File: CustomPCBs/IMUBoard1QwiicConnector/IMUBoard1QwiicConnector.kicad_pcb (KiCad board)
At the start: 2 copper layers, 11.1 x 17.7 mm, 14 parts, among them J1 Conn_01x04_Pin, Y1 32.768kHz

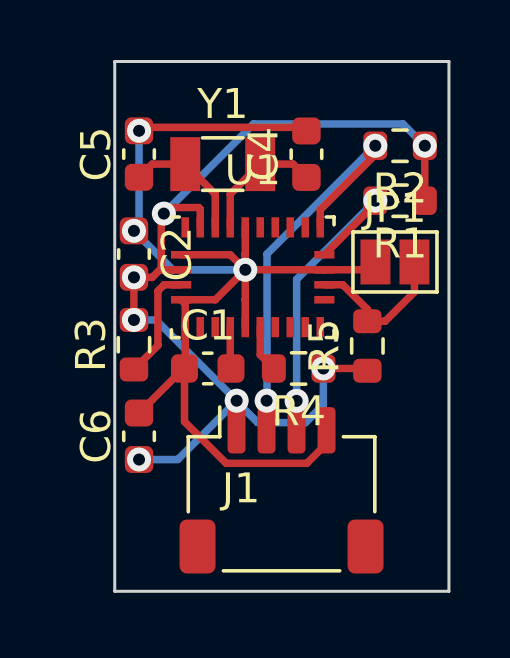
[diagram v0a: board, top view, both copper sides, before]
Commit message: Updating smallest IMU board
Will probably make it even smaller by hardwiring PS0, PS1 and SDO pins.
And maybe even the connector can go to give room for a cable bundle of 4
wires soldered to the board directly.
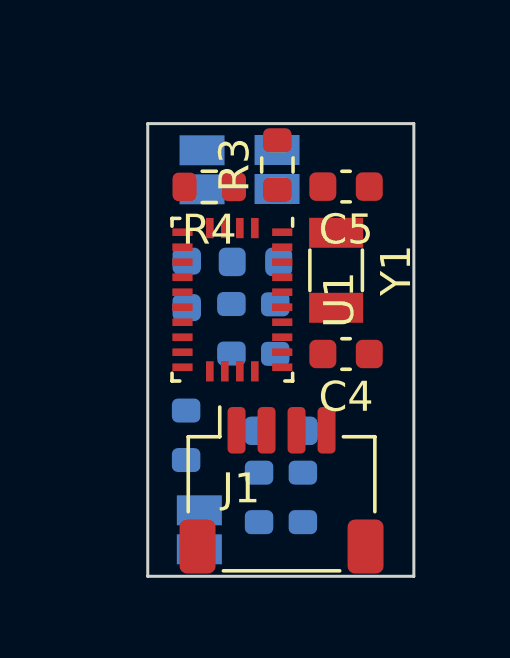
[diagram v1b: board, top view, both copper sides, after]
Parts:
- added JP2: SolderJumper_2_Open, Jumper:SolderJumper-2_P1.3mm_Open_Pad1.0x1.5mm, B.Cu at (97.1, 99.8)
- added JP3: SolderJumper_2_Open, Jumper:SolderJumper-2_P1.3mm_Open_Pad1.0x1.5mm, B.Cu at (99.6, 99.8)
- added R6: 10k, Resistor_SMD:R_0603_1608Metric, B.Cu at (98.1, 105.1)
- added R7: 10k, Resistor_SMD:R_0603_1608Metric, B.Cu at (99.6, 105.1)
- C1, C2, C6, JP1, R1, R2, R5: moved to B.Cu
- moved R2 12.6 mm to (99.0, 110.7), turned to 90 degrees
- moved JP1 11.1 mm to (97.0, 111.8), turned to 90 degrees
- moved R1 10.4 mm to (100.5, 110.7), turned to 90 degrees
- moved R3 7.66 mm to (99.6, 99.7)
- moved C5 6.98 mm to (101.9, 100.4), turned to 180 degrees
- moved C4 6.79 mm to (101.9, 106.0), turned to 180 degrees
- moved R4 6.75 mm to (97.4, 100.4)
- moved R5 6.73 mm to (96.6, 108.7)
- moved Y1 5.18 mm to (101.6, 103.2), turned to -90 degrees
- moved C6 4.73 mm to (99.8, 108.5), turned to 0 degrees
- moved C2 4.06 mm to (98.9, 102.9), turned to 180 degrees
- moved C1 2.89 mm to (96.6, 103.6), turned to 90 degrees
- moved U1 1.01 mm to (98.1, 104.1), turned to -90 degrees
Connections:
- U1 pad 5: GND -> PS1
- U1 pad 6: GND -> PS0
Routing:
- net GND: track 38.3 -> 0.00 mm, vias 3 -> 0
- net +3V3: track 34.6 -> 0.00 mm, vias 7 -> 0
- net SDA: track 14.8 -> 0.00 mm, vias 2 -> 0
- net SCL: track 11.2 -> 0.00 mm, vias 2 -> 0
- net SDO: track 5.14 -> 0.00 mm
- net Net-(U1-CLKSEL1/XOUT32): track 4.25 -> 0.00 mm
- net Net-(U1-XIN32): track 4.25 -> 0.00 mm
- net Net-(U1-BOOTN): track 3.81 -> 0.00 mm
- net Net-(U1-NRST): track 1.57 -> 0.00 mm
- net Net-(U1-CAP): track 1.39 -> 0.00 mm
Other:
- board size 11.1 x 17.7 mm -> 8.9 x 15.1 mm

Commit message: Making the IMU board on the finger tip smaller
Just saving work to continue at lunch, will use 4 layer pcb for the
board to be as small as possible
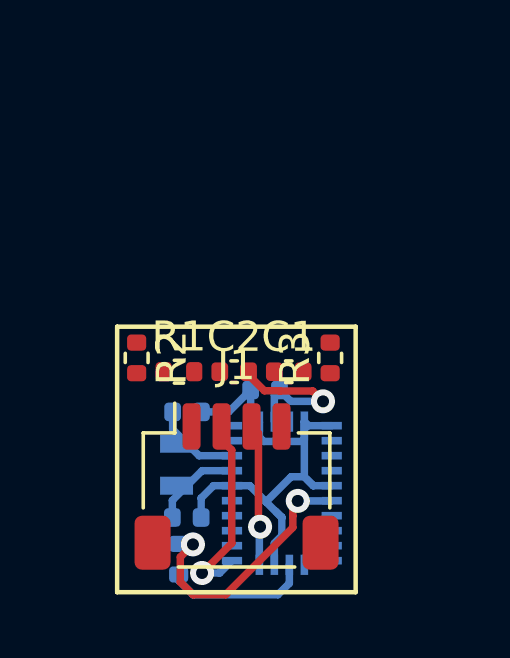
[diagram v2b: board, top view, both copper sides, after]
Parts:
- removed JP1, JP2, JP3: SolderJumper_2_Open, Jumper:SolderJumper-2_P1.3mm_Open_Pad1.0x1.5mm
- removed R5, R6, R7: 10k, Resistor_SMD:R_0603_1608Metric
- C1, C2: footprint Capacitor_SMD:C_0603_1608Metric -> Capacitor_SMD:C_0402_1005Metric; moved to F.Cu
- C4, C5: footprint Capacitor_SMD:C_0603_1608Metric -> Capacitor_SMD:C_0402_1005Metric; moved to B.Cu
- C6: footprint Capacitor_SMD:C_0603_1608Metric -> Capacitor_SMD:C_0402_1005Metric
- R1, R2: footprint Resistor_SMD:R_0603_1608Metric -> Resistor_SMD:R_0402_1005Metric; moved to F.Cu
- R3: footprint Resistor_SMD:R_0603_1608Metric -> Resistor_SMD:R_0402_1005Metric
- R4: footprint Resistor_SMD:R_0603_1608Metric -> Resistor_SMD:R_0402_1005Metric; moved to B.Cu
- U1: moved to B.Cu
- Y1: footprint Crystal:Crystal_SMD_3215-2Pin_3.2x1.5mm -> Crystal:Crystal_SMD_2012-2Pin_2.0x1.2mm; moved to B.Cu
- moved R4 12.5 mm to (96.3, 112.8), turned to 90 degrees
- moved C5 9.19 mm to (96.6, 107.9), turned to 0 degrees
- moved Y1 8.38 mm to (96.3, 109.6), turned to 90 degrees
- moved C4 7.61 mm to (96.6, 111.4), turned to 0 degrees
- moved R3 6.67 mm to (101.4, 106.1)
- moved U1 6.66 mm to (99.8, 110.6)
- moved R2 6.19 mm to (95.0, 106.1), turned to -90 degrees
- moved R1 5.88 mm to (96.4, 106.5), turned to 0 degrees
- moved C1 4.48 mm to (100.0, 106.5), turned to 0 degrees
- moved C2 3.73 mm to (98.2, 106.5), turned to 0 degrees
- moved J1 1.51 mm to (98.3, 110.4)
- moved C6 1.46 mm to (99.2, 107.2), turned to 180 degrees
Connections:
- U1 pad 17: SDO -> +3V3
- U1 pad 5: PS1 -> GND
- U1 pad 6: PS0 -> GND
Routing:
- net GND: track 0.00 -> 17.5 mm
- net +3V3: track 0.00 -> 10.5 mm, vias 0 -> 1
- net Net-(U1-NRST): track 0.00 -> 8.37 mm, vias 0 -> 2
- net SDA: track 0.00 -> 6.60 mm, vias 0 -> 1
- net SCL: track 0.00 -> 4.74 mm, vias 0 -> 1
- net Net-(U1-CLKSEL1/XOUT32): track 0.00 -> 2.97 mm
- net Net-(U1-XIN32): track 0.00 -> 2.92 mm
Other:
- board outline removed
- copper layers 2 -> 4

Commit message: Smaller IMU board achieved, needs centering
So it is possible to get a JST and BNO085 in a board around 9x8mm. This
looks good enough for the finger tip
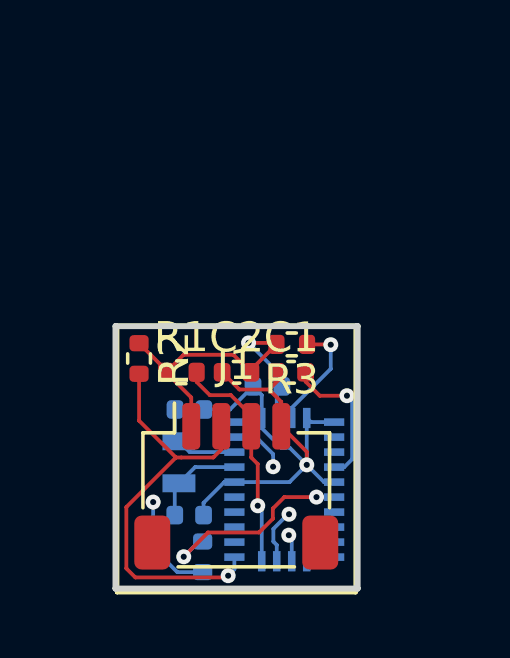
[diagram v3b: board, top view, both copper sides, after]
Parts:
- moved R3 1.36 mm to (100.1, 105.6), turned to 180 degrees
- moved R4 0.80 mm to (97.2, 112.7)
- moved C6 0.14 mm to (99.3, 107.0)
- moved U1 0.14 mm to (99.9, 110.5)
- moved C4 0.11 mm to (96.7, 111.3)
- moved C5 0.11 mm to (96.7, 107.8)
- moved Y1 0.11 mm to (96.4, 109.6)
- moved C1 0.08 mm to (100.1, 106.6)
- moved C2 0.08 mm to (98.3, 106.6)
- moved R1 0.08 mm to (96.4, 106.6)
- moved R2 0.08 mm to (95.0, 106.1)
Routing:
- net +3V3: track 10.5 -> 18.5 mm, vias 1 -> 4
- net SDA: track 6.60 -> 14.3 mm
- net Net-(U1-CAP): track 0.00 -> 4.78 mm, vias 0 -> 1
- net Net-(U1-BOOTN): track 0.00 -> 3.78 mm, vias 0 -> 1
- net GND: track 17.5 -> 20.9 mm, vias 0 -> 2
- net SCL: track 4.74 -> 7.61 mm
- net Net-(U1-NRST): track 8.37 -> 6.88 mm
- added copper zone on In1.Cu, net +3V3
- added copper zone on In2.Cu, net GND
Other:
- board outline added: 8.1 x 8.8 mm

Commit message: 9x8mm format achieved with everything centered
This allows some margin on the sides for a 3D printed insert
to stabilize the board on the glove finger tips
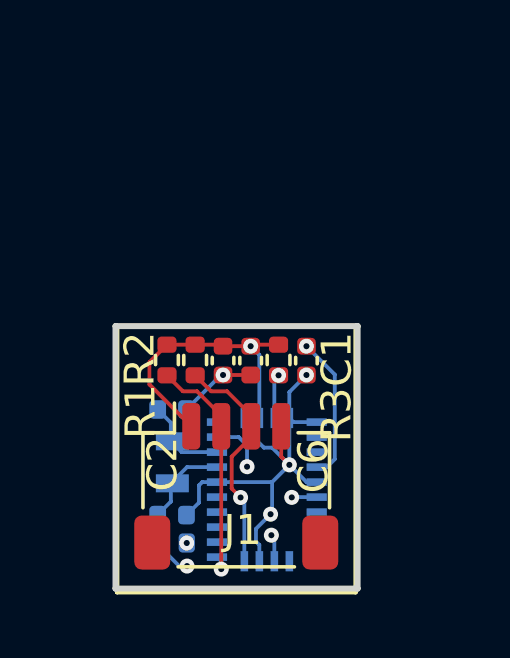
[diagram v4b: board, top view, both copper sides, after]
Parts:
- C6: moved to F.Cu
- moved R4 1.14 mm to (96.1, 112.2), turned to 180 degrees
- moved C6 1.03 mm to (98.8, 106.2), turned to -90 degrees
- moved R2 0.93 mm to (96.0, 106.2)
- moved R3 0.68 mm to (99.7, 106.2), turned to 90 degrees
- moved C1 0.64 mm to (100.6, 106.2), turned to 90 degrees
- moved R1 0.62 mm to (96.9, 106.2), turned to -90 degrees
- moved C2 0.60 mm to (97.8, 106.2), turned to 90 degrees
- moved C5 0.58 mm to (96.1, 107.8)
- moved U1 0.58 mm to (99.3, 110.5)
- moved C4 0.57 mm to (96.1, 111.3)
- moved Y1 0.22 mm to (96.1, 109.6)
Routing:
- net SDA: track 14.3 -> 7.94 mm
- net +3V3: track 18.5 -> 12.6 mm
- net Net-(U1-NRST): track 6.88 -> 11.0 mm
- net Net-(U1-BOOTN): track 3.78 -> 1.48 mm
- net GND: track 20.9 -> 19.1 mm, vias 2 -> 4
